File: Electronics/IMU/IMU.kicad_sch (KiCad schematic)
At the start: 3 parts, among them J1 Conn_01x02, U1 TEENSY 4.0, U2 Adafruit BNO085

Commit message: Added 4.7uF caps to FT232RL on controller.
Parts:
- J1: LCSC (none) -> C7494857
- U1: LCSC (none) -> C2897377
- U2: LCSC (none) -> C350307
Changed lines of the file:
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@@
+      (effects (font (size 1.27 1.27)) hide)
+    )
+    (property "LCSC" "C7494857" (at 130.81 51.435 0)
       (effects (font (size 1.27 1.27)) hide)
     )
@@
     )
     (property "Datasheet" "" (at 123.825 142.24 0)
+      (effects (font (size 1.27 1.27)) hide)
+    )
+    (property "LCSC" "C350307" (at 123.825 146.05 0)
       (effects (font (size 1.27 1.27)) hide)
     )
@@
       (effects (font (size 1.27 1.27)) hide)
     )
+    (property "LCSC" "C2897377" (at 115.57 181.61 0)
+      (effects (font (size 1.27 1.27)) hide)
+    )

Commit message: Removed JLCPCB part numbers for Teensy and BNO085 connectors. Added JLCPCB part number for 4.7uF capacitor. Generated JLCPCB manufacturing files for all boards.
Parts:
- U1: LCSC C2897377 -> (none)
- U2: LCSC C350307 -> (none)
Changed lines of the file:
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@@
       (effects (font (size 1.27 1.27)) hide)
     )
-    (property "LCSC" "C350307" (at 123.825 146.05 0)
+    (property "LCSC" "" (at 123.825 146.05 0)
       (effects (font (size 1.27 1.27)) hide)
     )
@@
       (effects (font (size 1.27 1.27)) hide)
     )
-    (property "LCSC" "C2897377" (at 115.57 181.61 0)
+    (property "LCSC" "" (at 115.57 181.61 0)
       (effects (font (size 1.27 1.27)) hide)
     )

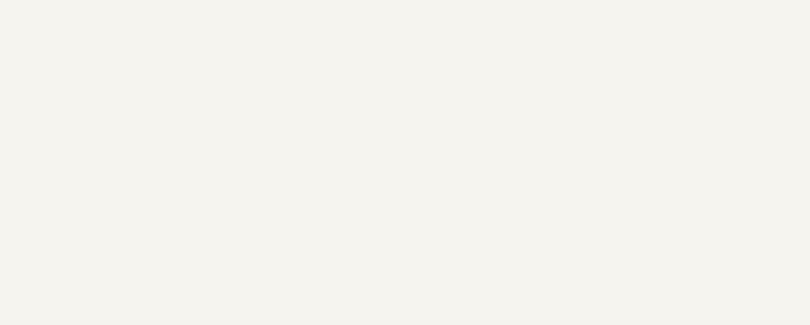
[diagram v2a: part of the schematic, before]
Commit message: Added fiducials to all boards.
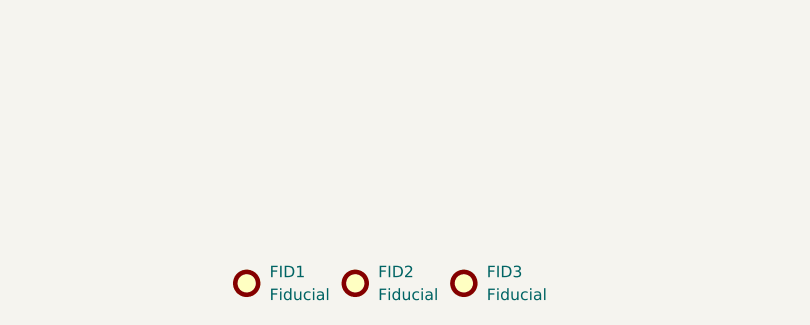
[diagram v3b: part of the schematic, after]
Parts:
- added FID1, FID2, FID3: Fiducial, Fiducial:Fiducial_0.5mm_Mask1mm, symbol Mechanical:Fiducial
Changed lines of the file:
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@@
   (title_block
     (title "Tandem Leveller IMU")
-    (date "2025-02-20")
+    (date "2025-03-13")
     (rev "V1.0")
     (company "(C) andy@britishideas.com 2025")
@@
     )
   )
+  (symbol (lib_id "Mechanical:Fiducial") (at 136.525 187.96 0) (unit 1)
+    (in_bom yes) (on_board yes) (dnp no) (fields_autoplaced)
+    (property "Reference" "FID1" (at 139.065 186.69 0)
+      (effects (font (size 1.27 1.27)) (justify left))
+    )
+    (property "Value" "Fiducial" (at 139.065 189.23 0)
+      (effects (font (size 1.27 1.27)) (justify left))
+    )
+    (property "Footprint" "Fiducial:Fiducial_0.5mm_Mask1mm" (at 136.525 187.96 0)
+      (effects (font (size 1.27 1.27)) hide)
+    )
+    (property "Datasheet" "~" (at 136.525 187.96 0)
+      (effects (font (size 1.27 1.27)) hide)
+    )
+    (instances
+      (project "IMU"
+        (path "/28b3abbf-dc5e-455e-8b3e-7e603a3b7233"
+          (reference "FID1") (unit 1)
+        )
+      )
+    )
+  )
+  (symbol (lib_id "Mechanical:Fiducial") (at 160.655 187.96 0) (unit 1)
+    (in_bom yes) (on_board yes) (dnp no) (fields_autoplaced)
+    (property "Reference" "FID3" (at 163.195 186.69 0)
+      (effects (font (size 1.27 1.27)) (justify left))
+    )
+    (property "Value" "Fiducial" (at 163.195 189.23 0)
+      (effects (font (size 1.27 1.27)) (justify left))
+    )
+    (property "Footprint" "Fiducial:Fiducial_0.5mm_Mask1mm" (at 160.655 187.96 0)
+      (effects (font (size 1.27 1.27)) hide)
+    )
+    (property "Datasheet" "~" (at 160.655 187.96 0)
+      (effects (font (size 1.27 1.27)) hide)
+    )
+    (instances
+      (project "IMU"
+        (path "/28b3abbf-dc5e-455e-8b3e-7e603a3b7233"
+          (reference "FID3") (unit 1)
+        )
+      )
+    )
+  )
   (symbol (lib_id "power:GND") (at 143.51 104.14 0) (unit 1)
     (in_bom yes) (on_board yes) (dnp no)
@@
         )
       )
+    )
+  )
+  (symbol (lib_id "Mechanical:Fiducial") (at 148.59 187.96 0) (unit 1)
+    (in_bom yes) (on_board yes) (dnp no) (fields_autoplaced)
+    (property "Reference" "FID2" (at 151.13 186.69 0)
+      (effects (font (size 1.27 1.27)) (justify left))
+    )
+    (property "Value" "Fiducial" (at 151.13 189.23 0)
+      (effects (font (size 1.27 1.27)) (justify left))
+    )
+    (property "Footprint" "Fiducial:Fiducial_0.5mm_Mask1mm" (at 148.59 187.96 0)
+      (effects (font (size 1.27 1.27)) hide)
+    )
+    (property "Datasheet" "~" (at 148.59 187.96 0)
+      (effects (font (size 1.27 1.27)) hide)
+    )
+    (instances
+      (project "IMU"
+        (path "/28b3abbf-dc5e-455e-8b3e-7e603a3b7233"
+          (reference "FID2") (unit 1)
+        )
+      )
